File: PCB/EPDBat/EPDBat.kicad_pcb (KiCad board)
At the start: 2 copper layers, 70 x 70 mm, 51 parts, among them J1 Conn_01x26, J10 JST-PH-SM3-TBT, J2 Shelly, J3 USB-PROG, J7 USB-C-Socket-V, Q1 BSS138, Q2 CJ2301, Q3 C179347, Q4 C179347, U1 TP4054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

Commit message: Tracked
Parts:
- removed Q4: C179347, RevK:SOT-323_SC-70
- removed R15: 10K, RevK:R_0402
- moved D5 16.2 mm to (110.5, 93.5)
- moved R14 15.6 mm to (111.6, 87.9), turned to -90 degrees
- moved U1 12.6 mm to (103.8, 102.3), turned to -90 degrees
- moved R17 11.7 mm to (107.4, 93.6), turned to 90 degrees
- moved Q2 11.3 mm to (109.6, 96.5), turned to -90 degrees
- moved R12 9.69 mm to (112.1, 95.1)
- moved R16 9.13 mm to (107.4, 95.4), turned to 90 degrees
- moved Q3 7.26 mm to (109.6, 87.8)
- moved C19 6.61 mm to (112.2, 90.8), turned to -90 degrees
- moved R13 5.12 mm to (104.2, 104.9)
- moved C5 4.91 mm to (97.6, 98.4), turned to 0 degrees
- moved U2 2.69 mm to (109.3, 90.8)
- moved J10 1.14 mm to (90.5, 103.3), turned to -90 degrees
- moved C2 0.81 mm to (95.8, 98.6), turned to -90 degrees
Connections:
- net EPDPWR renamed EPDP
- D5 pad 2: PWR -> VBUS
- Q2 pad 1: PWR -> VBUS
- R12 pad 1: PWR -> VBUS
- R16 pad 1: Net-(Q4-D) -> VBAT
- U4 pad 14: unconnected-(U4-GPIO10-Pad14) -> STAT
- U4 pad 20: unconnected-(U4-GPIO16-Pad20) -> GND
- U4 pad 31: ADCFET -> unconnected-(U4-GPIO35-Pad31)
- U4 pad 5: STAT -> unconnected-(U4-GPIO1-Pad5)
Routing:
- net +3V3: track 7.56 -> 61.3 mm, vias 0 -> 2
- net VBAT: track 0.00 -> 25.4 mm
- net ADC: track 0.00 -> 21.2 mm, vias 0 -> 2
- net GND: track 9.84 -> 22.9 mm, vias 14 -> 15
- net D+: track 36.8 -> 27.6 mm
- net VBUS: track 19.1 -> 27.5 mm
- net Net-(D5-K): track 0.00 -> 7.63 mm
- net EPDP: track 0.00 -> 7.46 mm
- net STAT: track 0.00 -> 6.39 mm, vias 0 -> 2
- net D-: track 47.7 -> 51.0 mm
- net VEPD: track 23.2 -> 25.7 mm
- net Net-(U1-PROG): track 0.00 -> 1.41 mm
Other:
- board text added: "+"
- board text added: "-"
- board text added: "10"
- board text added: "5060634238168"
- board text added: "AB"
- board text added: "EPDP"
- board text added: "Made in China for Andrews&Arnold Ltd"
- board text removed: "35"
- board text removed: "5060634238XXX"
- board text removed: "A"
- board text removed: "ADCPWR"
- board text removed: "EPDPWR"

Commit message: BTN added
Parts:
- added J4: Conn_01x02, RevK:PinHeader_1x02_P2.54mm_Vertical, F.Cu at (89.0, 76.2)
- turned JP1 to 0 degrees
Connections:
- R1 pad 1: Net-(JP1-A) -> Net-(JP1-B)
- R2 pad 2: Net-(JP1-B) -> Net-(JP1-A)
- U4 pad 31: unconnected-(U4-GPIO35-Pad31) -> RGB
- U4 pad 32: RGB -> BTN
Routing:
- net BTN: track 0.00 -> 18.0 mm, vias 0 -> 1
- net RGB: track 21.5 -> 23.5 mm
- net +3V3: track 61.3 -> 59.8 mm
- net Net-(JP1-B): track 2.59 -> 3.19 mm
- net Net-(JP1-A): track 3.19 -> 2.59 mm
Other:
- board text added: "35"
- board text added: "BAT"
- board text added: "BTN"

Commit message: As ordered
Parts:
- J10: value JST-PH-SM3-TBT -> JST-PH-SM3-TB; footprint Connector_JST:JST_PH_B2B-PH-SM4-TB_1x02-1MP_P2.00mm_Vertical -> Connector_JST:JST_PH_S2B-PH-SM4-TB_1x02-1MP_P2.00mm_Horizontal
- moved C5 2.61 mm to (100.2, 98.2)
- moved C2 2.60 mm to (98.4, 98.6)
- moved J10 1.30 mm to (91.8, 103.2), turned to 90 degrees
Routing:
- net +3V3: track 59.8 -> 62.3 mm
- net VBAT: track 25.4 -> 26.2 mm

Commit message: ESD
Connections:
- net +3V3 renamed +3.3V

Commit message: ESD
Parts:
- added D6: ~, RevK:DFN1006-2L, F.Cu at (91.1, 79.4)
- U2: footprint RevK:SOT-23-5 -> Package_TO_SOT_SMD:SOT-23-5
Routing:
- net BTN: track 18.0 -> 19.9 mm

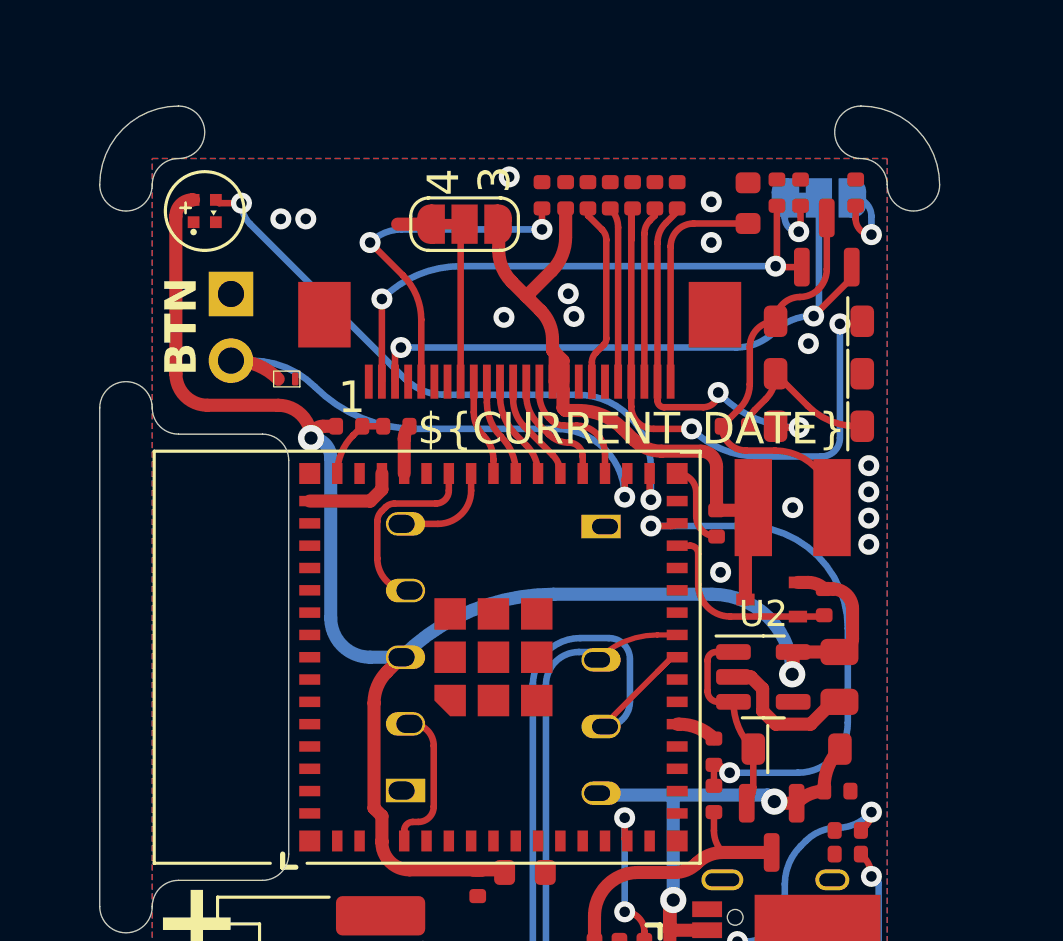
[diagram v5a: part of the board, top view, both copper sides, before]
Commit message: Moved connector to reduce slack
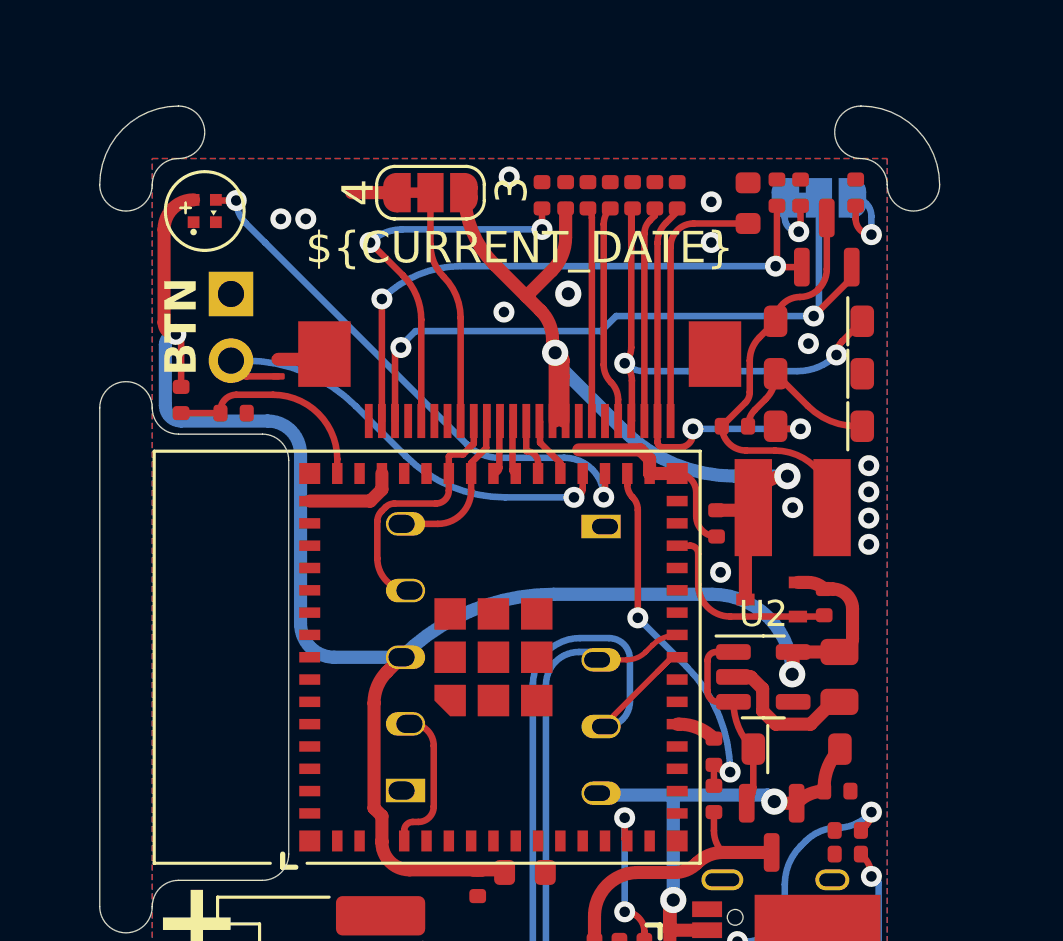
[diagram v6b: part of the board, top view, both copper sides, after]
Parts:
- moved R3 6.48 mm to (87.1, 80.2), turned to -90 degrees
- moved C6 6.22 mm to (89.1, 80.7)
- moved JP2 1.77 mm to (96.6, 72.3)
- moved J1 1.50 mm to (100.0, 79.7)
- moved D6 0.54 mm to (90.8, 79.0), turned to -90 degrees
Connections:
- J2 pad 4: Net-(J2-Rx) -> BUSY
- J2 pad 5: Net-(J2-Tx) -> RST
- U4 pad 29: ADC -> unconnected-(U4-GPIO34-Pad29)
- U4 pad 31: RGB -> GND
- U4 pad 32: BTN -> ADC
- U4 pad 33: MOSI -> RGB
- U4 pad 34: CLK -> BTN
- U4 pad 35: CS -> MOSI
- U4 pad 36: DC -> CLK
- U4 pad 37: RST -> CS
- U4 pad 38: BUSY -> DC
- U4 pad 39: Net-(J2-Tx) -> RST
- U4 pad 40: Net-(J2-Rx) -> BUSY
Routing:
- net VEPD: track 25.5 -> 33.8 mm, vias 0 -> 2
- net Net-(J2-Rx): track 7.29 -> 0.00 mm
- net ADC: track 21.2 -> 14.2 mm
- net BUSY: track 3.69 -> 9.95 mm
- net Net-(U4-EN): track 2.89 -> 8.12 mm
- net GND: track 22.9 -> 27.5 mm, vias 15 -> 14
- net Net-(J2-Tx): track 3.97 -> 0.00 mm
- net Net-(D3-K): track 22.7 -> 19.2 mm
- net Net-(J1-Pin_8): track 5.85 -> 8.99 mm
- net RGB: track 23.5 -> 20.7 mm
- net +3.3V: track 62.3 -> 65.1 mm
- net RST: track 3.72 -> 6.22 mm
- net MOSI: track 4.52 -> 2.33 mm
- net CS: track 4.13 -> 2.08 mm
- net BTN: track 19.9 -> 17.9 mm
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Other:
- board text removed: "1"
